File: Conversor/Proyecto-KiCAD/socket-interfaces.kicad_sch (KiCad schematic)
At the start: 23 parts, among them J7 DIMM100, P10 Header GPIO, P5 Header 7X2, P6 Header UART, P7 Header I2C, P8 Header PWM, P9 Header ADC, SW1 Switch, SW2 Switch, SW3 Switch, SW4 Switch

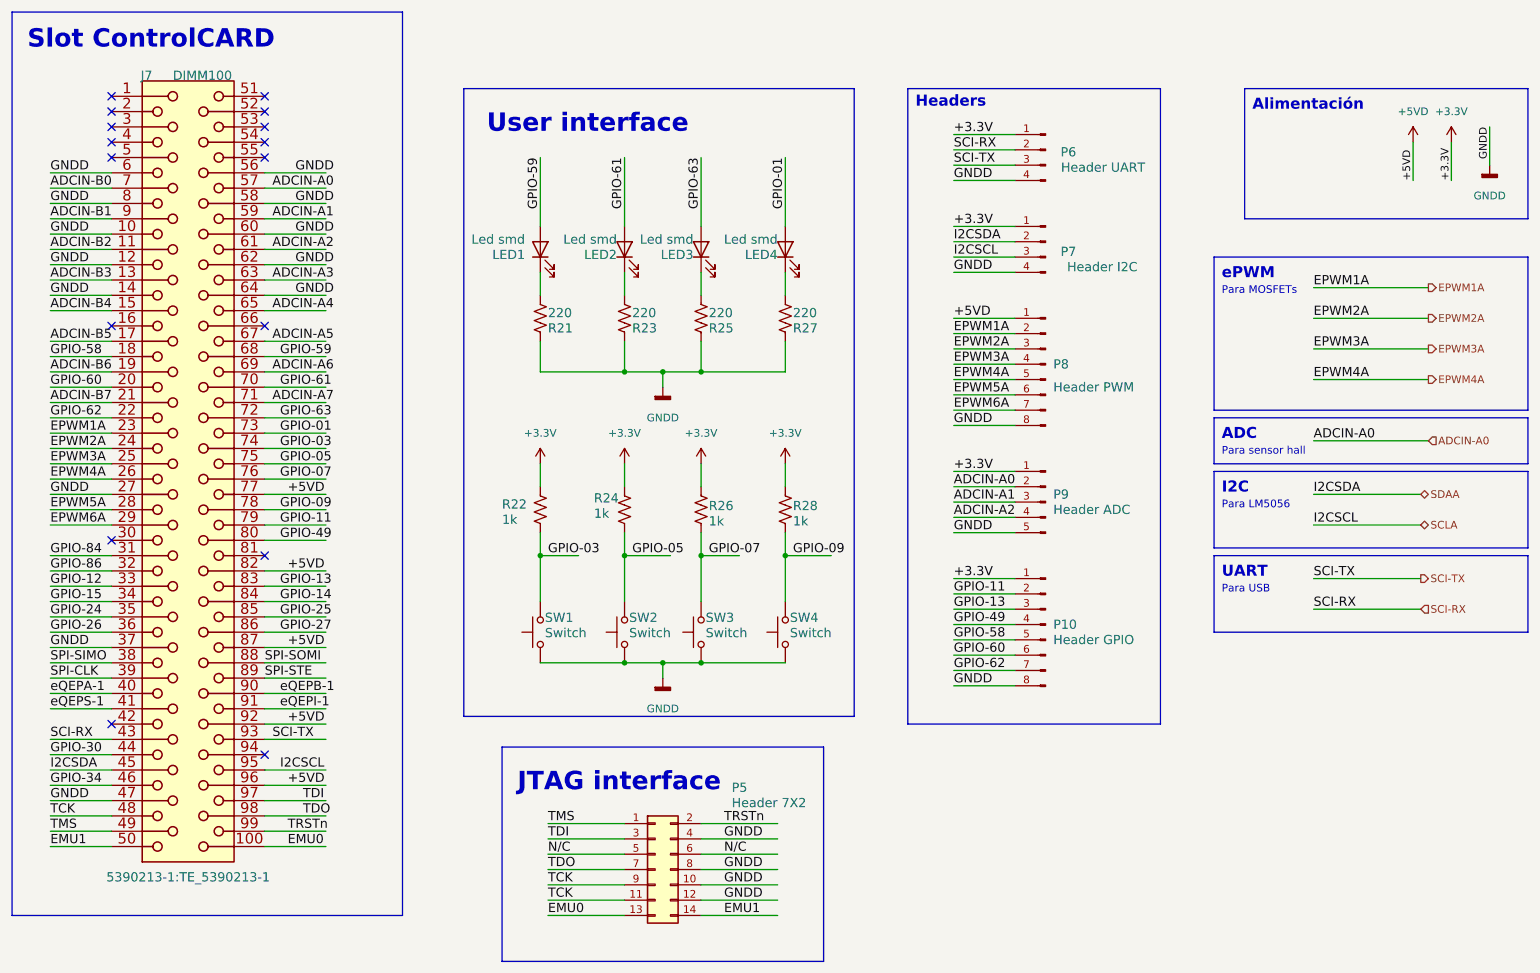
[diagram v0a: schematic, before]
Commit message: Comenzar a asignar footprints a todos los componentes
- Agregado un header para conectar el módulo de tarjeta SD de Arduino
por SPI
- Los GNDs conectados por resistencias nulas son para conectar los GNDs
en caso de que fuera necesario
- Agregar una nota de aplicaión de aislación para I2C (creo que como
estan conectados SDAO y SDAI está bien)
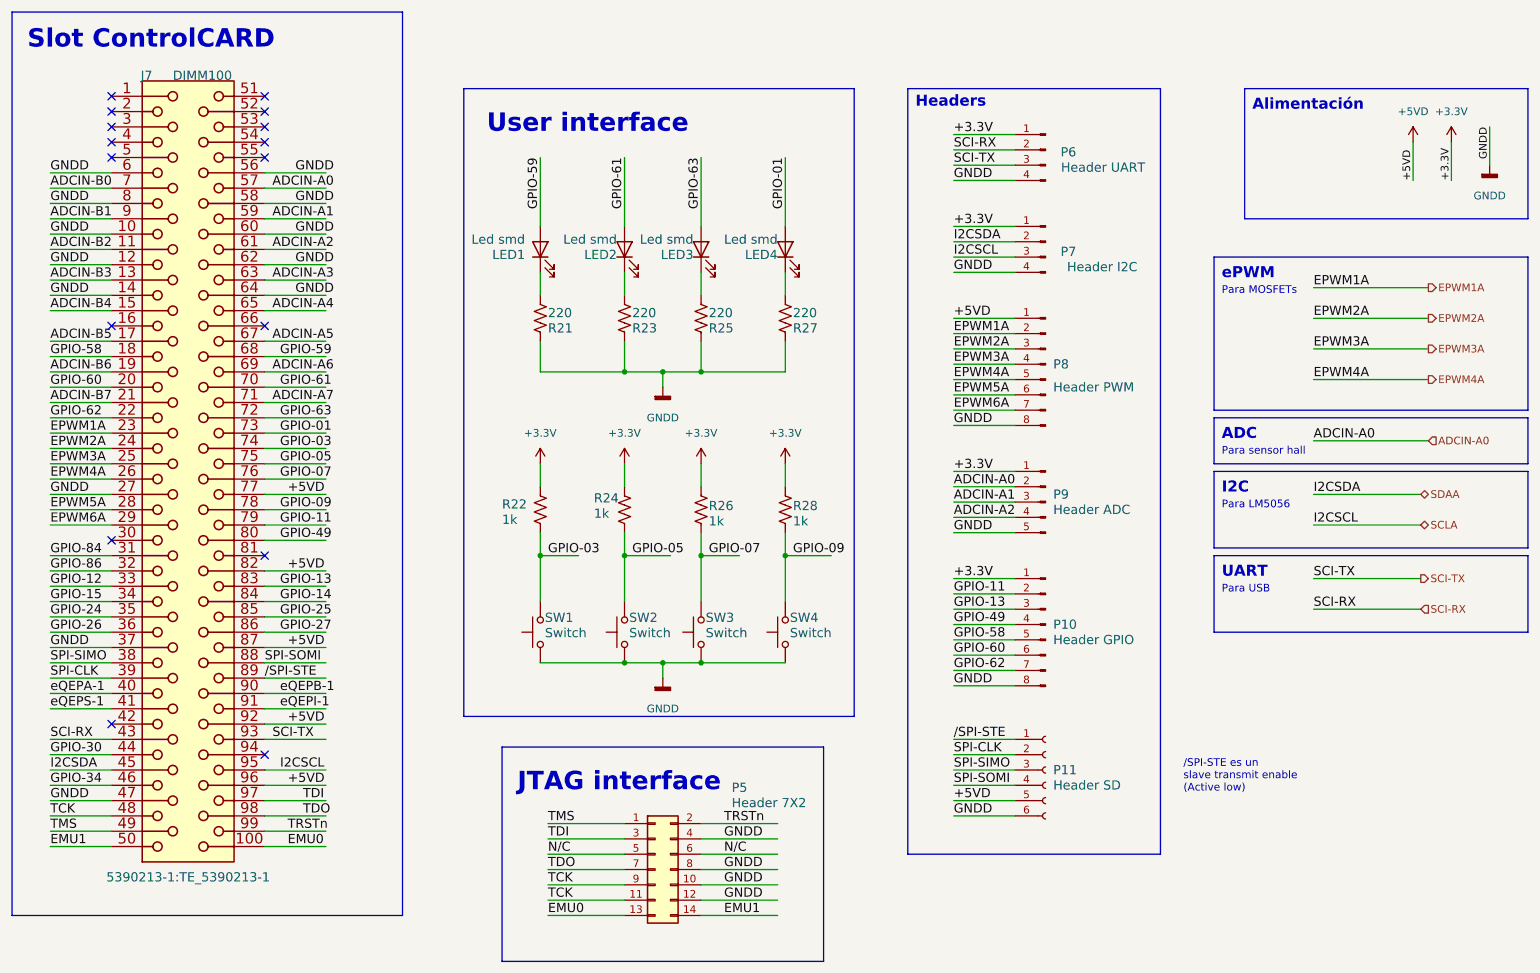
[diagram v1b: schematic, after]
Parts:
- added P11: Header SD, Connector_PinSocket_2.54mm:PinSocket_1x06_P2.54mm_Horizontal, symbol Connector:Conn_01x06_Female
- LED1, LED2, LED3, LED4: footprint (none) -> Diode_SMD:D_1206_3216Metric_Pad1.42x1.75mm_HandSolder
- P10, P8: footprint (none) -> Connector_PinHeader_2.54mm:PinHeader_1x08_P2.54mm_Horizontal
- P5: footprint (none) -> Connector_PinSocket_2.54mm:PinSocket_2x07_P2.54mm_Vertical
- P6, P7: footprint (none) -> Connector_PinHeader_2.54mm:PinHeader_1x04_P2.54mm_Horizontal
- P9: footprint (none) -> Connector_PinHeader_2.54mm:PinHeader_1x05_P2.54mm_Horizontal
- R21, R22, R23, R24, R25, R26, R27, R28: footprint (none) -> Resistor_SMD:R_1206_3216Metric_Pad1.30x1.75mm_HandSolder
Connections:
- net +5VD: now also P11.5 (Pin_5)
- net GNDD: now also P11.6 (Pin_6)
- net SPI-CLK: now also P11.2 (Pin_2)
- net SPI-SIMO: now also P11.3 (Pin_3)
- net SPI-SOMI: now also P11.4 (Pin_4)
- net SPI-STE renamed /SPI-STE
- net /SPI-STE: now also P11.1 (Pin_1)
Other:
- note added: "/SPI-STE es un slave transmit enable (Active low)"

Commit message: Comenzar el layout de componentes de la PCB
- Todos los componentes con footprints asignados (preliminar)
- Organizados los componentes de la placa adaptadora en el esquema del
PCB (usando como guia aproximada la placa adaptadora)
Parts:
- P10, P8: footprint Connector_PinHeader_2.54mm:PinHeader_1x08_P2.54mm_Horizontal -> Connector_PinHeader_2.54mm:PinHeader_1x08_P2.54mm_Vertical
- P6, P7: footprint Connector_PinHeader_2.54mm:PinHeader_1x04_P2.54mm_Horizontal -> Connector_PinHeader_2.54mm:PinHeader_1x04_P2.54mm_Vertical
- P9: footprint Connector_PinHeader_2.54mm:PinHeader_1x05_P2.54mm_Horizontal -> Connector_PinHeader_2.54mm:PinHeader_1x05_P2.54mm_Vertical
- SW1, SW2, SW3, SW4: footprint (none) -> Button_Switch_THT:SW_PUSH_6mm
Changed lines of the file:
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@@
       (effects (font (size 1.524 1.524)) (justify left bottom))
     )
-    (property "Footprint" "Connector_PinHeader_2.54mm:PinHeader_1x04_P2.54mm_Horizontal" (id 2) (at 190.5 38.1 0)
+    (property "Footprint" "Connector_PinHeader_2.54mm:PinHeader_1x04_P2.54mm_Vertical" (id 2) (at 190.5 38.1 0)
       (effects (font (size 1.27 1.27)) hide)
     )
@@
       (effects (font (size 1.524 1.524)) (justify right top))
     )
-    (property "Footprint" "" (id 2) (at 142.24 118.11 0)
+    (property "Footprint" "Button_Switch_THT:SW_PUSH_6mm" (id 2) (at 142.24 118.11 0)
       (effects (font (size 1.27 1.27)) hide)
     )
@@
       (effects (font (size 1.524 1.524)) (justify left bottom))
     )
-    (property "Footprint" "Connector_PinHeader_2.54mm:PinHeader_1x04_P2.54mm_Horizontal" (id 2) (at 190.5 53.34 0)
+    (property "Footprint" "Connector_PinHeader_2.54mm:PinHeader_1x04_P2.54mm_Vertical" (id 2) (at 190.5 53.34 0)
       (effects (font (size 1.27 1.27)) hide)
     )
@@
       (effects (font (size 1.524 1.524)) (justify right top))
     )
-    (property "Footprint" "" (id 2) (at 101.6 118.11 0)
+    (property "Footprint" "Button_Switch_THT:SW_PUSH_6mm" (id 2) (at 101.6 118.11 0)
       (effects (font (size 1.27 1.27)) hide)
     )
@@
       (effects (font (size 1.524 1.524)) (justify right))
     )
-    (property "Footprint" "Connector_PinHeader_2.54mm:PinHeader_1x05_P2.54mm_Horizontal" (id 2) (at 190.5 96.52 0)
+    (property "Footprint" "Connector_PinHeader_2.54mm:PinHeader_1x05_P2.54mm_Vertical" (id 2) (at 190.5 96.52 0)
       (effects (font (size 1.27 1.27)) hide)
     )
@@
       (effects (font (size 1.524 1.524)) (justify right))
     )
-    (property "Footprint" "Connector_PinHeader_2.54mm:PinHeader_1x08_P2.54mm_Horizontal" (id 2) (at 190.5 116.84 0)
+    (property "Footprint" "Connector_PinHeader_2.54mm:PinHeader_1x08_P2.54mm_Vertical" (id 2) (at 190.5 116.84 0)
       (effects (font (size 1.27 1.27)) hide)
     )
@@
       (effects (font (size 1.524 1.524)) (justify right))
     )
-    (property "Footprint" "Connector_PinHeader_2.54mm:PinHeader_1x08_P2.54mm_Horizontal" (id 2) (at 190.5 73.66 0)
+    (property "Footprint" "Connector_PinHeader_2.54mm:PinHeader_1x08_P2.54mm_Vertical" (id 2) (at 190.5 73.66 0)
       (effects (font (size 1.27 1.27)) hide)
     )
@@
       (effects (font (size 1.524 1.524)) (justify right top))
     )
-    (property "Footprint" "" (id 2) (at 115.57 118.11 0)
+    (property "Footprint" "Button_Switch_THT:SW_PUSH_6mm" (id 2) (at 115.57 118.11 0)
       (effects (font (size 1.27 1.27)) hide)
     )
@@
       (effects (font (size 1.524 1.524)) (justify right top))
     )
-    (property "Footprint" "" (id 2) (at 128.27 118.11 0)
-      (effects (font (size 1.27 1.27)) hide)
-    )
+    (property "Footprint" "Button_Switch_THT:SW_PUSH_6mm" (id 2) (at 128.27 118.11 0)
+      (effects (font (size 1.27 1.27)) hide)
+    )
